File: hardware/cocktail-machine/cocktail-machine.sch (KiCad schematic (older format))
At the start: 18 parts

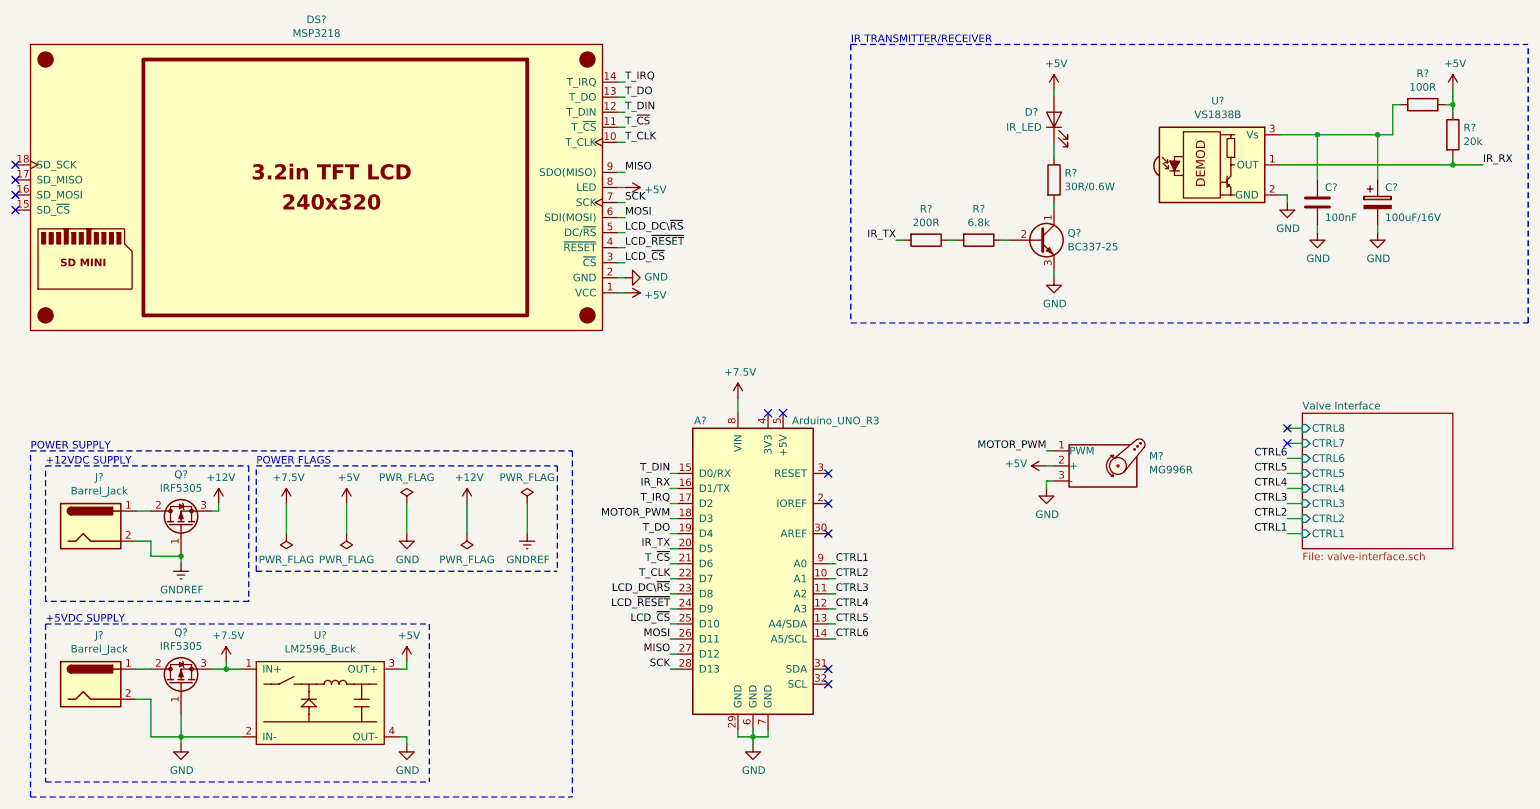
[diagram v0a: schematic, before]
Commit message: Use IR photodiode instead of IR receiver
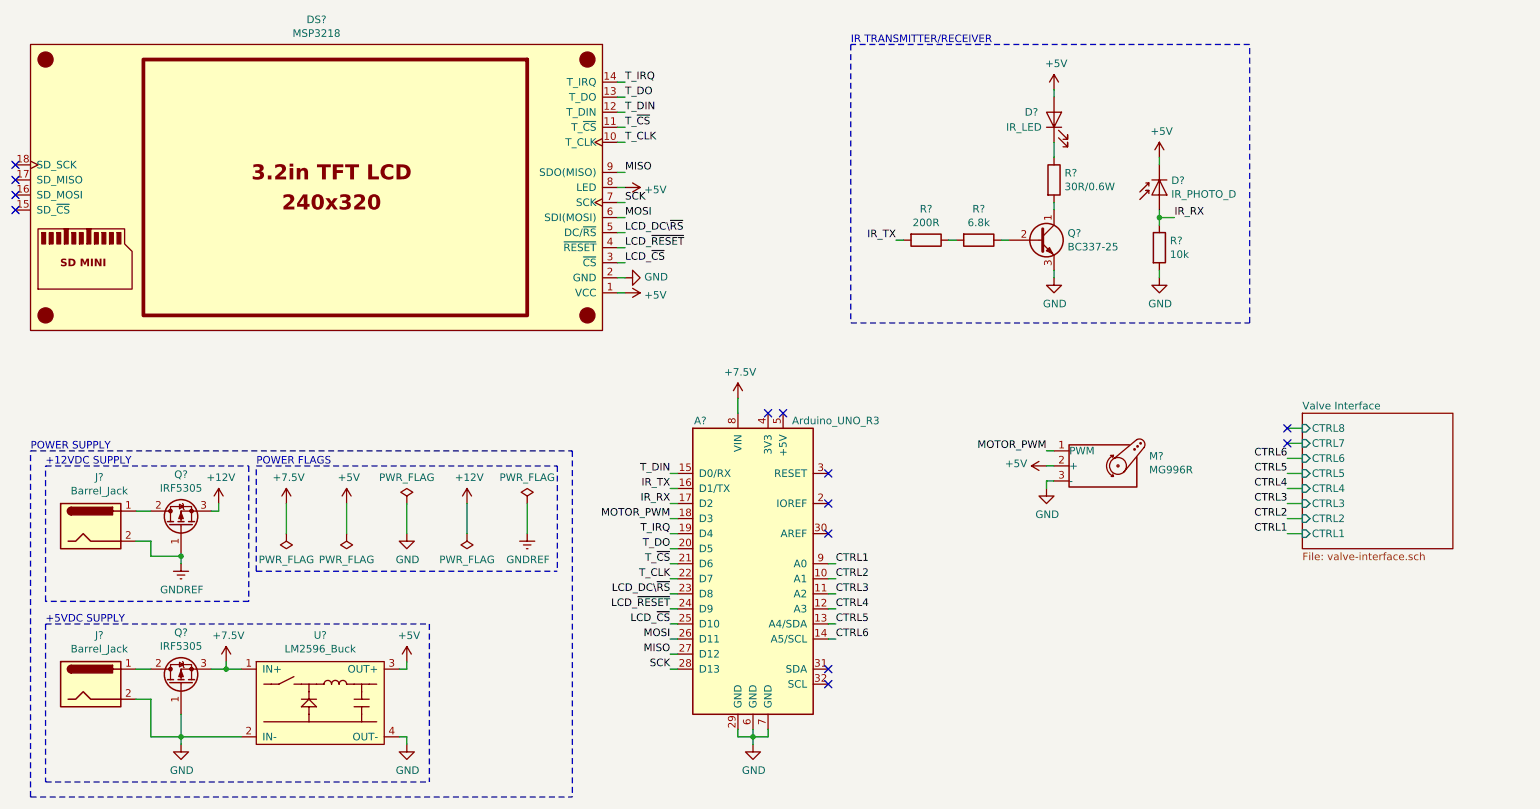
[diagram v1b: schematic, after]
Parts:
- removed C?: 100uF/16V, symbol Device:CP
- removed C?: 100nF, symbol Device:C
- removed R?: 100R, symbol Device:R
- removed R?: 20k, symbol Device:R
- removed U?: VS1838B, OptoDevice:Vishay_MOLD-3Pin, symbol Interface_Optical:TSDP341xx
- added D?: IR_PHOTO_D, symbol Device:D_Photo
- added R?: 10k, symbol Device:R
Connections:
- net +5V: now also D?.1 (K)
- net GND: now also R?.2
- net IR_RX: now also A?.17 (D2), D?.2 (A), R?.1; no longer A?.16 (D1/TX)
- net IR_TX: now also A?.16 (D1/TX); no longer A?.20 (D5)
- net T_DO: now also A?.20 (D5); no longer A?.19 (D4)
- net T_IRQ: now also A?.19 (D4); no longer A?.17 (D2)
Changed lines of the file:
@@
 Sheet 1 2
 Title "Cocktail Machine"
-Date "2020-04-30"
+Date "2020-05-10"
 Rev "1"
 Comp "Pesho & Valka Inc."
@@
 	1    0    0    -1
 $EndComp
-$Comp
-L Interface_Optical:TSDP341xx U?
-U 1 1 5E9465A8
-P 8750 2100
-F 0 "U?" H 8738 2525 50  0000 C CNN
-F 1 "VS1838B" H 8738 2434 50  0000 C CNN
-F 2 "OptoDevice:Vishay_MOLD-3Pin" H 8700 1725 50  0001 C CNN
-F 3 "http://www.vishay.com/docs/82667/tsdp341.pdf" H 9400 2400 50  0001 C CNN
-	1    8750 2100
-	1    0    0    -1
-$EndComp
-$Comp
-L Device:CP C?
-U 1 1 5E94758E
-P 9800 2350
-F 0 "C?" H 9850 2450 50  0000 L CNN
-F 1 "100uF/16V" H 9850 2250 50  0000 L CNN
-F 2 "" H 9838 2200 50  0001 C CNN
-F 3 "~" H 9800 2350 50  0001 C CNN
-	1    9800 2350
-	1    0    0    -1
-$EndComp
-Wire Wire Line
-	9150 2300 9200 2300
-Wire Wire Line
-	9200 2300 9200 2350
-$Comp
-L power:GND #PWR?
-U 1 1 5E9513E3
-P 9200 2350
-F 0 "#PWR?" H 9200 2100 50  0001 C CNN
-F 1 "GND" H 9205 2177 50  0000 C CNN
-F 2 "" H 9200 2350 50  0001 C CNN
-F 3 "" H 9200 2350 50  0001 C CNN
-	1    9200 2350
-	1    0    0    -1
-$EndComp
-$Comp
-L Device:R R?
-U 1 1 5E951E9B
-P 10100 1700
-F 0 "R?" V 9893 1700 50  0000 C CNN
-F 1 "100R" V 9984 1700 50  0000 C CNN
-F 2 "" V 10030 1700 50  0001 C CNN
-F 3 "~" H 10100 1700 50  0001 C CNN
-	1    10100 1700
-	0    1    1    0
-$EndComp
-$Comp
-L Device:R R?
-U 1 1 5E952138
-P 10300 1900
-F 0 "R?" H 10370 1946 50  0000 L CNN
-F 1 "20k" H 10370 1855 50  0000 L CNN
-F 2 "" V 10230 1900 50  0001 C CNN
-F 3 "~" H 10300 1900 50  0001 C CNN
-	1    10300 1900
-	1    0    0    -1
-$EndComp
-Text Label 10500 2100 0    50   ~ 0
+Text Label 8450 2450 0    50   ~ 0
 IR_RX
-Wire Wire Line
-	9150 2100 10300 2100
-Wire Wire Line
-	10300 2100 10300 2050
-Connection ~ 10300 2100
-Wire Wire Line
-	10300 2100 10500 2100
-Wire Wire Line
-	10300 1750 10300 1700
-Wire Wire Line
-	10300 1700 10250 1700
-Wire Wire Line
-	9150 1900 9400 1900
-$Comp
-L Device:C C?
-U 1 1 5E95CF9F
-P 9400 2350
-F 0 "C?" H 9450 2450 50  0000 L CNN
-F 1 "100nF" H 9450 2250 50  0000 L CNN
-F 2 "" H 9438 2200 50  0001 C CNN
-F 3 "~" H 9400 2350 50  0001 C CNN
-	1    9400 2350
-	1    0    0    -1
-$EndComp
-Wire Wire Line
-	9400 2200 9400 1900
-Connection ~ 9400 1900
-Wire Wire Line
-	9400 2500 9400 2550
-$Comp
-L power:GND #PWR?
-U 1 1 5E9605F1
-P 9400 2550
-F 0 "#PWR?" H 9400 2300 50  0001 C CNN
-F 1 "GND" H 9405 2377 50  0000 C CNN
-F 2 "" H 9400 2550 50  0001 C CNN
-F 3 "" H 9400 2550 50  0001 C CNN
-	1    9400 2550
-	1    0    0    -1
-$EndComp
-Wire Wire Line
-	9800 2200 9800 1900
-Wire Wire Line
-	9400 1900 9800 1900
-Wire Wire Line
-	9800 2500 9800 2550
-$Comp
-L power:GND #PWR?
-U 1 1 5E964CB4
-P 9800 2550
-F 0 "#PWR?" H 9800 2300 50  0001 C CNN
-F 1 "GND" H 9805 2377 50  0000 C CNN
-F 2 "" H 9800 2550 50  0001 C CNN
-F 3 "" H 9800 2550 50  0001 C CNN
-	1    9800 2550
-	1    0    0    -1
-$EndComp
-Wire Wire Line
-	9800 1900 9900 1900
-Wire Wire Line
-	9900 1900 9900 1700
-Wire Wire Line
-	9900 1700 9950 1700
-Connection ~ 9800 1900
-Wire Wire Line
-	10300 1700 10300 1600
-Connection ~ 10300 1700
-$Comp
-L power:+5V #PWR?
-U 1 1 5E9657E5
-P 10300 1600
-F 0 "#PWR?" H 10300 1450 50  0001 C CNN
-F 1 "+5V" H 10315 1773 50  0000 C CNN
-F 2 "" H 10300 1600 50  0001 C CNN
-F 3 "" H 10300 1600 50  0001 C CNN
-	1    10300 1600
-	1    0    0    -1
-$EndComp
 Wire Wire Line
 	7650 1650 7650 1600
@@
 Text Label 6600 2600 2    50   ~ 0
 IR_TX
+Text Label 5100 4350 2    50   ~ 0
+IR_RX
 Text Label 5100 4250 2    50   ~ 0
-IR_RX
-Text Label 5100 4650 2    50   ~ 0
 IR_TX
 NoConn ~ 6150 5450
@@
 NoConn ~ 6150 4350
 NoConn ~ 6150 4150
-Wire Notes Line
-	10800 3150 10800 1300
 $Comp
 L Connector:Barrel_Jack J?
@@
 Wire Wire Line
 	5150 4350 5100 4350
-Text Label 5100 4350 2    50   ~ 0
+Text Label 5100 4550 2    50   ~ 0
 T_IRQ
-Text Label 5100 4550 2    50   ~ 0
+Text Label 5100 4650 2    50   ~ 0
 T_DO
 Text Label 5100 4150 2    50   ~ 0
@@
 Wire Notes Line
 	6300 1300 6300 3150
-Wire Notes Line
-	6300 3150 10800 3150
-Wire Notes Line
-	6300 1300 10800 1300
 $Comp
 L Device:LED D?
@@
 	1    0    0    -1
 $EndComp
+$Comp
+L Device:D_Photo D?
+U 1 1 5EB8F707
+P 8350 2300
+F 0 "D?" V 8254 2221 50  0000 R CNN
+F 1 "IR_PHOTO_D" V 8345 2221 50  0000 R CNN
+F 2 "" H 8300 2300 50  0001 C CNN
+F 3 "~" H 8300 2300 50  0001 C CNN
+	1    8350 2300
+	0    -1   1    0
+$EndComp
+Wire Wire Line
+	8350 2100 8350 2050
+$Comp
+L power:+5V #PWR?
+U 1 1 5EB93ADC
+P 8350 2050
+F 0 "#PWR?" H 8350 1900 50  0001 C CNN
+F 1 "+5V" H 8365 2223 50  0000 C CNN
+F 2 "" H 8350 2050 50  0001 C CNN
+F 3 "" H 8350 2050 50  0001 C CNN
+	1    8350 2050
+	1    0    0    -1
+$EndComp
+Wire Wire Line
+	8350 2400 8350 2450
+$Comp
+L Device:R R?
+U 1 1 5EB96DF6
+P 8350 2650
+F 0 "R?" H 8420 2696 50  0000 L CNN
+F 1 "10k" H 8420 2605 50  0000 L CNN
+F 2 "" V 8280 2650 50  0001 C CNN
+F 3 "~" H 8350 2650 50  0001 C CNN
+	1    8350 2650
+	1    0    0    -1
+$EndComp
+Wire Wire Line
+	8350 2800 8350 2850
+$Comp
+L power:GND #PWR?
+U 1 1 5EB9A137
+P 8350 2850
+F 0 "#PWR?" H 8350 2600 50  0001 C CNN
+F 1 "GND" H 8355 2677 50  0000 C CNN
+F 2 "" H 8350 2850 50  0001 C CNN
+F 3 "" H 8350 2850 50  0001 C CNN
+	1    8350 2850
+	1    0    0    -1
+$EndComp
+Wire Wire Line
+	8350 2450 8450 2450
+Connection ~ 8350 2450
+Wire Wire Line
+	8350 2450 8350 2500
+Wire Notes Line
+	6300 3150 8950 3150
+Wire Notes Line
+	8950 3150 8950 1300
+Wire Notes Line
+	8950 1300 6300 1300
 $EndSCHEMATC

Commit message: Final schematic version
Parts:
- M7: renamed from M?; value MG996R -> SERVO
- gave numbers to parts that had none: 14

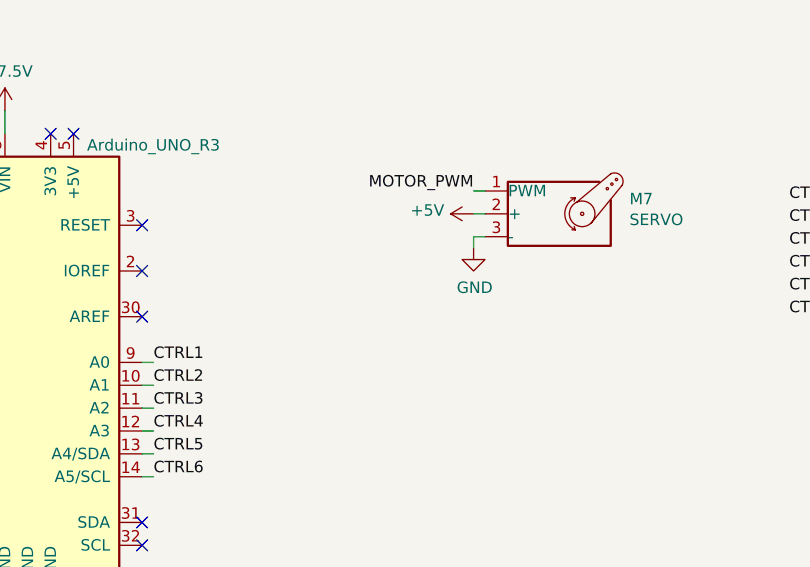
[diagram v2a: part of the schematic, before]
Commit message: Add smoothing capacitor to servo power lines
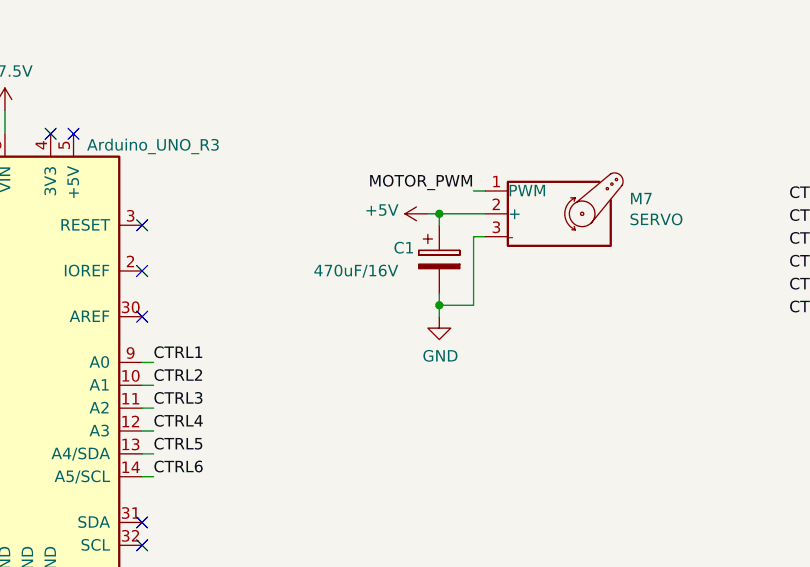
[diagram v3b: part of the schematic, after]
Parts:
- added C1: 470uF/16V, symbol Device:CP
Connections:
- net +5V: now also C1.1
- net GND: now also C1.2
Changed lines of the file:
@@
 Sheet 1 2
 Title "Cocktail Machine"
-Date "2020-06-06"
+Date "2020-06-10"
 Rev "1"
 Comp "Pesho & Valka Inc."
@@
 	1    0    0    -1
 $EndComp
-Wire Wire Line
-	7650 4200 7600 4200
-Wire Wire Line
-	7600 4200 7600 4250
 $Comp
 L power:GND #PWR018
 U 1 1 5EBAB346
-P 7600 4250
-F 0 "#PWR018" H 7600 4000 50  0001 C CNN
-F 1 "GND" H 7605 4077 50  0000 C CNN
-F 2 "" H 7600 4250 50  0001 C CNN
-F 3 "" H 7600 4250 50  0001 C CNN
-	1    7600 4250
-	1    0    0    -1
-$EndComp
-Wire Wire Line
-	7650 4100 7600 4100
+P 7450 4550
+F 0 "#PWR018" H 7450 4300 50  0001 C CNN
+F 1 "GND" H 7455 4377 50  0000 C CNN
+F 2 "" H 7450 4550 50  0001 C CNN
+F 3 "" H 7450 4550 50  0001 C CNN
+	1    7450 4550
+	1    0    0    -1
+$EndComp
 Wire Wire Line
 	7650 4000 7600 4000
@@
 L power:+5V #PWR017
 U 1 1 5EBAD44E
-P 7600 4100
-F 0 "#PWR017" H 7600 3950 50  0001 C CNN
-F 1 "+5V" V 7615 4228 50  0000 L CNN
-F 2 "" H 7600 4100 50  0001 C CNN
-F 3 "" H 7600 4100 50  0001 C CNN
-	1    7600 4100
+P 7400 4100
+F 0 "#PWR017" H 7400 3950 50  0001 C CNN
+F 1 "+5V" V 7415 4228 50  0000 L CNN
+F 2 "" H 7400 4100 50  0001 C CNN
+F 3 "" H 7400 4100 50  0001 C CNN
+	1    7400 4100
 	0    -1   -1   0
 $EndComp
@@
 Wire Notes Line
 	8950 1300 6300 1300
+$Comp
+L Device:CP C1
+U 1 1 5EE17430
+P 7450 4300
+F 0 "C1" H 7250 4350 50  0000 L CNN
+F 1 "470uF/16V" H 6900 4250 50  0000 L CNN
+F 2 "" H 7488 4150 50  0001 C CNN
+F 3 "~" H 7450 4300 50  0001 C CNN
+	1    7450 4300
+	1    0    0    -1
+$EndComp
+Wire Wire Line
+	7400 4100 7450 4100
+Wire Wire Line
+	7450 4450 7450 4500
+Wire Wire Line
+	7450 4500 7600 4500
+Wire Wire Line
+	7600 4500 7600 4200
+Wire Wire Line
+	7600 4200 7650 4200
+Connection ~ 7450 4500
+Wire Wire Line
+	7450 4500 7450 4550
+Wire Wire Line
+	7450 4150 7450 4100
+Connection ~ 7450 4100
+Wire Wire Line
+	7450 4100 7650 4100
 $EndSCHEMATC
